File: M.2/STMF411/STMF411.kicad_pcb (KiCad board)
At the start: 2 copper layers, 22 x 26 mm, 26 parts, among them M1 M.2_Key_E, Q1 2N7002, SW1 RESET, U1 XC6206P332MR, U2 STM32F411CCUx, Y1 16 MHz

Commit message: prettify files a lil bit
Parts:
- moved C10 25.8 mm to (27.0, 28.4)
- moved C11 25.8 mm to (34.9, 30.0)
- moved C12 25.8 mm to (33.5, 37.9)
- moved C13 25.8 mm to (25.5, 29.9)
- moved C15 25.8 mm to (23.9, 36.1)
- moved C2 25.8 mm to (19.6, 30.1)
- moved C3 25.8 mm to (22.2, 30.1)
- moved C5 25.8 mm to (32.0, 44.4)
- moved C6 25.8 mm to (30.7, 42.9)
- moved H1 25.8 mm to (28.4, 19.1)
- moved L1 25.8 mm to (35.9, 22.6)
- moved M1 25.8 mm to (28.4, 49.1)
- moved Q1 25.8 mm to (19.6, 27.9)
- moved R1 25.8 mm to (18.4, 30.2)
- moved R3 25.8 mm to (31.0, 38.7)
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
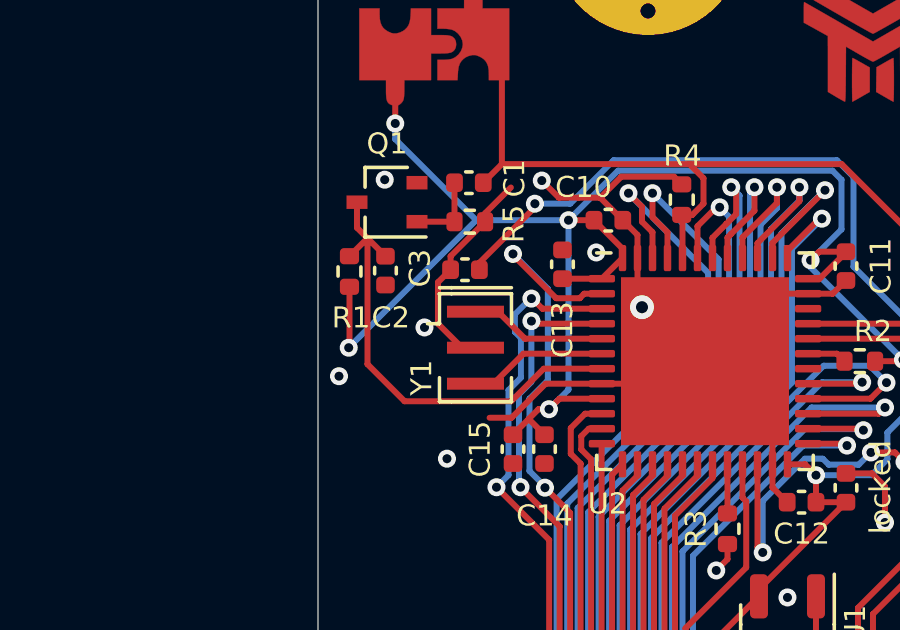
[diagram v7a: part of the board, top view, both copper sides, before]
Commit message: change up logo's to nicer ones on modules, update iss
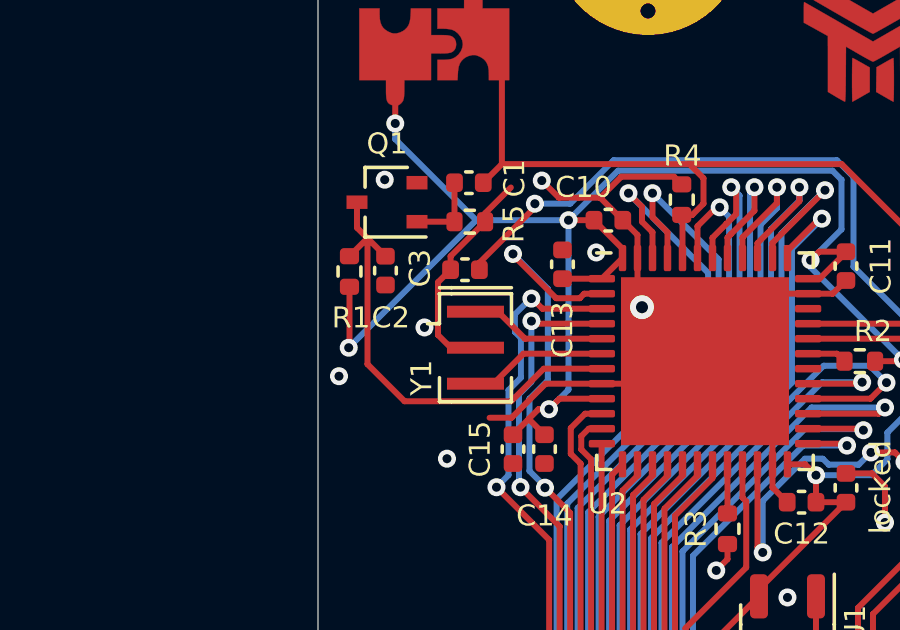
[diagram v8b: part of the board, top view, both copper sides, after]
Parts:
- added Ref**: Val**, silk:text, B.Cu at (28.4, 33.2)
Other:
- board text removed: "MUD Project M.2 Carrierboard STMF411 Edition Designed by Pat"
